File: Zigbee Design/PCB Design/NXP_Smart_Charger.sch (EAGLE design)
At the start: 91 parts, among them IC1 MID400, IC2 MID400, IC3 LMV358, IC4 LMV358, Q1 2222A, Q2 2222A

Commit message: NXP fixes
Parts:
- removed BUTTONS: (no value), SparkFun-Connectors:CONN_04
- removed LEDS: (no value), SparkFun-Connectors:CONN_10"
- removed R32: 2.0k, SparkFun-Resistors:2.0KOHM-0603-1/10W-5%
- removed R37, R38, R39, R40: 10, SparkFun-Resistors:10OHM-0603-1/10W-1%
- removed R42, R43: 75, SparkFun-Resistors:75KOHM-0603-1/10W-1%
- added J4: (no value), SparkFun-Connectors:CONN_08"
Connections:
- removed net CLK: JN5168.DIO16
- removed net FORCE_START: BUTTONS.1, JN5168.DIO0, R34.1
- removed net FORCE_STOP: BUTTONS.2, JN5168.DIO1, R32.1
- removed net L7: R39.2
- removed net L8: R40.2
- removed net N$18: LEDS.7, R37.1
- removed net N$46: JN5168.DIO9
- removed net N$47: JN5168.DIO10
- removed net N$50: LEDS.6, R38.1
- removed net N$51: LEDS.5, R42.1
- removed net N$52: LEDS.4, R39.1
- removed net N$54: LEDS.2, R43.1
- removed net N$55: JN5168.RESETN
- removed net N$56: JN5168.DIO13
- removed net N$75: LEDS.3, R40.1
- removed net SDA: JN5168.DIO17
- new net BUTTON1: J4.5, JN5168.DIO0, R31.1
- new net BUTTON2: J4.4, JN5168.DIO1, R34.1
- net BUTTON3: no longer BUTTONS.3, R31.1
- net GND: now also J4.1; no longer LEDS.1, R32.2
- net L1: now also JN5168.DIO17
- net L2: now also JN5168.DIO16
- net L3: now also JN5168.RESETN
- net L4: now also JN5168.DIO13; no longer R37.2
- net L5: now also JN5168.DIO10; no longer R38.2
- net L6: now also JN5168.DIO9; no longer R42.2
- net L9: no longer R43.2
- net N$14: now also J4.8; no longer LEDS.10
- net N$15: now also J4.7; no longer LEDS.9
- net N$16: now also J4.6; no longer LEDS.8
- net N$93: now also J4.2; no longer BUTTONS.4
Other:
- moved on the sheet: R31, R34, R35

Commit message: changes
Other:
- note removed: "Check power lines on board are correct thickness- especially 3v and GND"
- note removed: "DOUBLE CHECK TX/RX WIRING"
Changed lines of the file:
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@@
 <text x="-165.6" y="38.12" size="3.81" layer="94">for NXP JN5169</text>
 <text x="-119.38" y="223.52" size="6.4516" layer="94">NXP JN5168 Module</text>
-<text x="-73.66" y="160.02" size="1.778" layer="91">DOUBLE CHECK TX/RX WIRING</text>
-<text x="-236.22" y="154.94" size="1.778" layer="91">Check power lines on board are correct thickness- especially 3v and GND</text>
 </plain>
 <instances>
@@
 <pinref part="JN5168" gate="G$1" pin="DIO16"/>
 <wire x1="-91.44" y1="205.74" x2="-78.74" y2="205.74" width="0.1524" layer="91"/>
+<label x="-86.36" y="205.74" size="1.778" layer="95"/>
 </segment>
 </net>
@@
 <pinref part="JN5168" gate="G$1" pin="DIO17"/>
 <wire x1="-91.44" y1="208.28" x2="-78.74" y2="208.28" width="0.1524" layer="91"/>
+<label x="-86.36" y="208.28" size="1.778" layer="95"/>
 </segment>
 </net>
@@
 <pinref part="JN5168" gate="G$1" pin="DIO9"/>
 <wire x1="-104.14" y1="177.8" x2="-104.14" y2="170.18" width="0.1524" layer="91"/>
-<label x="-104.14" y="167.64" size="1.778" layer="95" rot="R90"/>
 </segment>
 </net>
@@
 <pinref part="JN5168" gate="G$1" pin="DIO10"/>
 <wire x1="-101.6" y1="177.8" x2="-101.6" y2="170.18" width="0.1524" layer="91"/>
-<label x="-101.6" y="167.64" size="1.778" layer="95" rot="R90"/>
 </segment>
 </net>
@@
 <pinref part="JN5168" gate="G$1" pin="DIO13"/>
 <wire x1="-91.44" y1="195.58" x2="-81.28" y2="195.58" width="0.1524" layer="91"/>
-<label x="-86.36" y="195.58" size="1.778" layer="95"/>
-</segment>
-</net>
+</segment>
+</net>

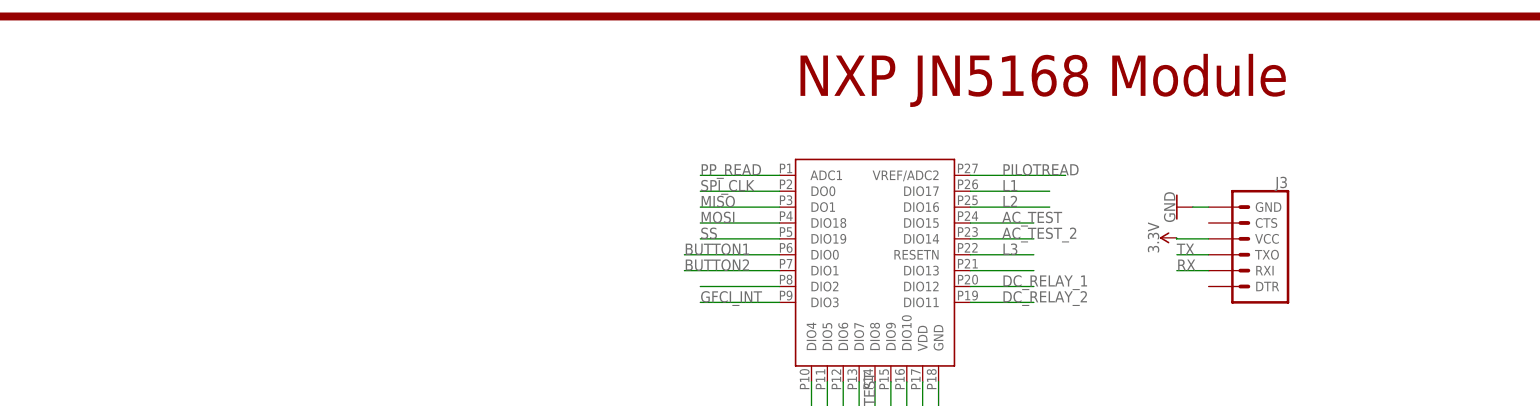
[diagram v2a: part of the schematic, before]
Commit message: added flash memory
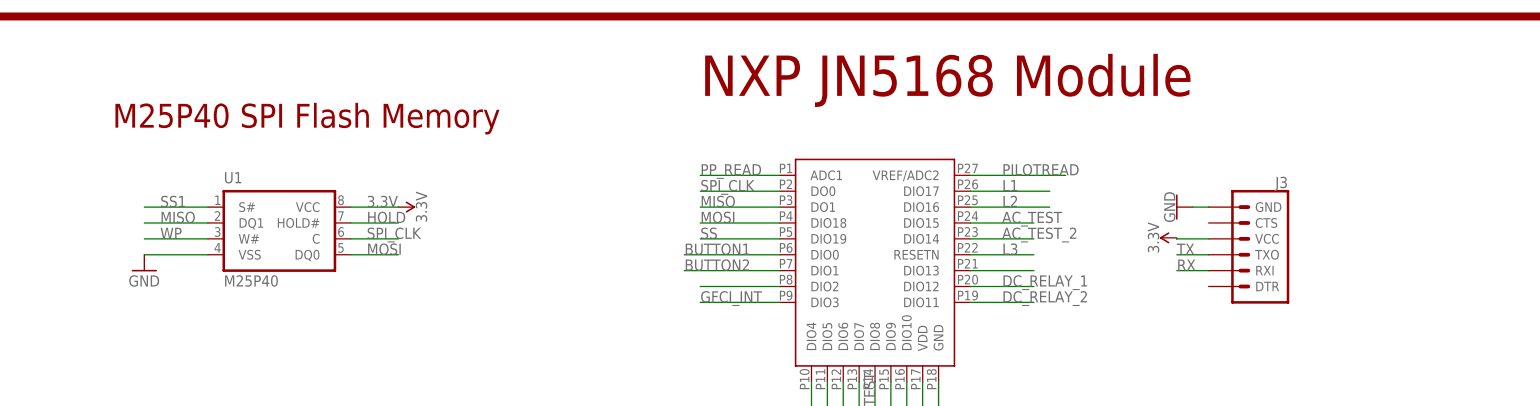
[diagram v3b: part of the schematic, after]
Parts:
- added U1: M25P40, Smart_Charger:M25P40
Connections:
- new net HOLD: U1.HOLD#
- new net SS1: U1.S#
- new net WP: U1.W#
- net 3.3V: now also U1.VCC
- net GND: now also U1.VSS
- net MISO: now also U1.DQ1
- net MOSI: now also U1.DQ0
- net SPI_CLK: now also U1.C
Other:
- note added: "M25P40 SPI Flash Memory"
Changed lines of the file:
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@@
 <part name="SUPPLY4" library="SparkFun-PowerSymbols" deviceset="3.3V" device=""/>
 <part name="J4" library="SparkFun-Connectors" deviceset="CONN_08" device="&quot;"/>
+<part name="U1" library="Smart_Charger" deviceset="M25P40" device=""/>
+<part name="SUPPLY1" library="SparkFun-PowerSymbols" deviceset="3.3V" device=""/>
+<part name="GND7" library="supply1" library_urn="urn:adsk.eagle:library:371" deviceset="GND" device=""/>
 </parts>
 <sheets>
@@
 Extended from Open EVSE project by Chris Howell</text>
 <text x="-165.6" y="38.12" size="3.81" layer="94">for NXP JN5169</text>
-<text x="-119.38" y="223.52" size="6.4516" layer="94">NXP JN5168 Module</text>
+<text x="-134.62" y="223.52" size="6.4516" layer="94">NXP JN5168 Module</text>
+<text x="-228.6" y="218.44" size="3.81" layer="94">M25P40 SPI Flash Memory</text>
 </plain>
 <instances>
@@
 <instance part="SUPPLY4" gate="G$1" x="-99.06" y="170.18" rot="R180"/>
 <instance part="J4" gate="G$1" x="-238.76" y="43.18"/>
+<instance part="U1" gate="G$1" x="-203.2" y="203.2"/>
+<instance part="SUPPLY1" gate="G$1" x="-182.88" y="205.74" rot="R270"/>
+<instance part="GND7" gate="1" x="-223.52" y="195.58"/>
 </instances>
 <busses>
@@
 <label x="-134.62" y="205.74" size="1.778" layer="95"/>
 </segment>
+<segment>
+<pinref part="U1" gate="G$1" pin="DQ1"/>
+<wire x1="-213.36" y1="203.2" x2="-223.52" y2="203.2" width="0.1524" layer="91"/>
+<label x="-220.98" y="203.2" size="1.778" layer="95"/>
+</segment>
 </net>
 <net name="MOSI" class="0">
@@
 <wire x1="-121.92" y1="203.2" x2="-134.62" y2="203.2" width="0.1524" layer="91"/>
 <label x="-134.62" y="203.2" size="1.778" layer="95"/>
+</segment>
+<segment>
+<pinref part="U1" gate="G$1" pin="DQ0"/>
+<wire x1="-190.5" y1="198.12" x2="-182.88" y2="198.12" width="0.1524" layer="91"/>
+<label x="-187.96" y="198.12" size="1.778" layer="95"/>
 </segment>
 </net>
@@
 <wire x1="-231.14" y1="35.56" x2="-231.14" y2="33.02" width="0.1524" layer="91"/>
 </segment>
+<segment>
+<pinref part="U1" gate="G$1" pin="VSS"/>
+<wire x1="-213.36" y1="198.12" x2="-223.52" y2="198.12" width="0.1524" layer="91"/>
+<pinref part="GND7" gate="1" pin="GND"/>
+</segment>
 </net>
 <net name="BUTTON3" class="0">
@@
 <wire x1="-99.06" y1="177.8" x2="-99.06" y2="170.18" width="0.1524" layer="91"/>
 <pinref part="SUPPLY4" gate="G$1" pin="3.3V"/>
+</segment>
+<segment>
+<pinref part="U1" gate="G$1" pin="VCC"/>
+<wire x1="-190.5" y1="205.74" x2="-182.88" y2="205.74" width="0.1524" layer="91"/>
+<label x="-187.96" y="205.74" size="1.778" layer="95"/>
+<pinref part="SUPPLY1" gate="G$1" pin="3.3V"/>
 </segment>
 </net>
@@
 <pinref part="WATTMETER" gate="G$1" pin="3"/>
 </segment>
+<segment>
+<pinref part="U1" gate="G$1" pin="C"/>
+<wire x1="-190.5" y1="200.66" x2="-182.88" y2="200.66" width="0.1524" layer="91"/>
+<label x="-187.96" y="200.66" size="1.778" layer="95"/>
+</segment>
 </net>
 <net name="L6" class="0">
@@
 </segment>
 </net>
+<net name="HOLD" class="0">
+<segment>
+<pinref part="U1" gate="G$1" pin="HOLD#"/>
+<wire x1="-190.5" y1="203.2" x2="-182.88" y2="203.2" width="0.1524" layer="91"/>
+<label x="-187.96" y="203.2" size="1.778" layer="95"/>
+</segment>
+</net>
+<net name="SS1" class="0">
+<segment>
+<pinref part="U1" gate="G$1" pin="S#"/>
+<wire x1="-213.36" y1="205.74" x2="-223.52" y2="205.74" width="0.1524" layer="91"/>
+<label x="-220.98" y="205.74" size="1.778" layer="95"/>
+</segment>
+</net>
+<net name="WP" class="0">
+<segment>
+<pinref part="U1" gate="G$1" pin="W#"/>
+<wire x1="-213.36" y1="200.66" x2="-223.52" y2="200.66" width="0.1524" layer="91"/>
+<label x="-220.98" y="200.66" size="1.778" layer="95"/>
+</segment>
+</net>

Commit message: added smartenit eagle file
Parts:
- removed J3: (no value), SparkFun-Connectors:6_PIN_SERIAL_TARGET
- removed U1: M25P40, Smart_Charger:M25P40
- added U$1: SPI_FLASH-X25XXSMD, SparkFun:SPI_FLASH-X25XXSMD
- added U$2: AVR_SPI_PROG2LOCK, SparkFun:AVR_SPI_PROG2LOCK
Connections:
- removed net BUTTON3: JN5168.DIO2
- removed net HOLD: U1.HOLD#
- removed net L4: JN5168.DIO13
- removed net L5: JN5168.DIO10
- removed net L6: JN5168.DIO9
- removed net L9: JN5168.DIO4
- removed net WP: U1.W#
- new net RESET: JN5168.RESETN
- net 3.3V: now also JN5168.VREF/ADC2, U$1.WP; no longer J3.VCC, U1.VCC
- net GND: now also U$1.GND; no longer J3.GND, U1.VSS
- net L3: now also JN5168.DIO13; no longer JN5168.RESETN
- net MISO: now also U$1.MISO; no longer U1.DQ1
- net MOSI: no longer U1.DQ0
- net PILOTREAD: now also JN5168.DIO2; no longer JN5168.VREF/ADC2
- net RX: no longer J3.RXI
- net SPI_CLK: no longer U1.C
- net SS1: now also JN5168.DIO4, U$1.CS; no longer U1.S#
- net TX: no longer J3.TXO
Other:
- note added: "W25X40CLSNIG-ND SPI Flash Memory"
- note removed: "M25P40 SPI Flash Memory"
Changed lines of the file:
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@@
 <part name="J2" library="SparkFun-Connectors" deviceset="CONN_02" device=""/>
 <part name="DC2" library="DCDCconverters" deviceset="NNM+-12V" device=""/>
-<part name="J3" library="SparkFun-Connectors" deviceset="6_PIN_SERIAL_TARGET" device=""/>
-<part name="SUPPLY3" library="SparkFun-PowerSymbols" deviceset="3.3V" device=""/>
-<part name="GND37" library="SparkFun-PowerSymbols" deviceset="GND" device=""/>
 <part name="JN5168" library="Smart_Charger" deviceset="NXP_JN5168-001-MO3" device=""/>
 <part name="GND6" library="supply1" library_urn="urn:adsk.eagle:library:371" deviceset="GND" device=""/>
 <part name="SUPPLY4" library="SparkFun-PowerSymbols" deviceset="3.3V" device=""/>
 <part name="J4" library="SparkFun-Connectors" deviceset="CONN_08" device="&quot;"/>
-<part name="U1" library="Smart_Charger" deviceset="M25P40" device=""/>
 <part name="SUPPLY1" library="SparkFun-PowerSymbols" deviceset="3.3V" device=""/>
 <part name="GND7" library="supply1" library_urn="urn:adsk.eagle:library:371" deviceset="GND" device=""/>
+<part name="SUPPLY6" library="SparkFun-PowerSymbols" deviceset="3.3V" device=""/>
+<part name="U$1" library="SparkFun" deviceset="SPI_FLASH-X25XX" device="SMD"/>
+<part name="SUPPLY9" library="SparkFun-PowerSymbols" deviceset="3.3V" device=""/>
+<part name="SUPPLY10" library="SparkFun-PowerSymbols" deviceset="3.3V" device=""/>
+<part name="U$2" library="SparkFun" deviceset="AVR_SPI_PROG2" device="LOCK"/>
 </parts>
 <sheets>
@@
 <text x="-165.6" y="38.12" size="3.81" layer="94">for NXP JN5169</text>
 <text x="-134.62" y="223.52" size="6.4516" layer="94">NXP JN5168 Module</text>
-<text x="-228.6" y="218.44" size="3.81" layer="94">M25P40 SPI Flash Memory</text>
+<text x="-228.6" y="218.44" size="3.81" layer="94">W25X40CLSNIG-ND SPI Flash Memory</text>
 </plain>
 <instances>
@@
 <instance part="J2" gate="G$1" x="36.5" y="-0.3"/>
 <instance part="DC2" gate="&gt;NAME" x="87.7" y="217.1"/>
-<instance part="J3" gate="G$1" x="-48.26" y="198.12" rot="MR0"/>
-<instance part="SUPPLY3" gate="G$1" x="-58.46" y="200.82" rot="R90"/>
-<instance part="GND37" gate="1" x="-58.42" y="205.74" rot="R270"/>
 <instance part="JN5168" gate="G$1" x="-78.74" y="190.5"/>
 <instance part="GND6" gate="1" x="-96.52" y="157.48"/>
 <instance part="SUPPLY4" gate="G$1" x="-99.06" y="170.18" rot="R180"/>
 <instance part="J4" gate="G$1" x="-238.76" y="43.18"/>
-<instance part="U1" gate="G$1" x="-203.2" y="203.2"/>
-<instance part="SUPPLY1" gate="G$1" x="-182.88" y="205.74" rot="R270"/>
+<instance part="SUPPLY1" gate="G$1" x="-175.26" y="205.74" rot="R270"/>
 <instance part="GND7" gate="1" x="-223.52" y="195.58"/>
+<instance part="SUPPLY6" gate="G$1" x="-76.2" y="210.82" rot="R270"/>
+<instance part="U$1" gate="G$1" x="-198.12" y="203.2"/>
+<instance part="SUPPLY9" gate="G$1" x="-223.52" y="200.66" rot="R90"/>
+<instance part="SUPPLY10" gate="G$1" x="-175.26" y="203.2" rot="R270"/>
+<instance part="U$2" gate="A" x="-45.72" y="175.26"/>
 </instances>
 <busses>
@@
 </segment>
 <segment>
-<pinref part="JN5168" gate="G$1" pin="VREF/ADC2"/>
-<wire x1="-91.44" y1="210.82" x2="-76.2" y2="210.82" width="0.1524" layer="91"/>
-<label x="-86.36" y="210.82" size="1.778" layer="95"/>
+<pinref part="JN5168" gate="G$1" pin="DIO2"/>
+<wire x1="-121.92" y1="193.04" x2="-134.62" y2="193.04" width="0.1524" layer="91"/>
+<label x="-137.16" y="193.04" size="1.778" layer="95"/>
 </segment>
 </net>
@@
 </segment>
 <segment>
-<pinref part="U1" gate="G$1" pin="DQ1"/>
 <wire x1="-213.36" y1="203.2" x2="-223.52" y2="203.2" width="0.1524" layer="91"/>
 <label x="-220.98" y="203.2" size="1.778" layer="95"/>
+<pinref part="U$1" gate="G$1" pin="MISO"/>
 </segment>
 </net>
@@
 </segment>
 <segment>
-<pinref part="U1" gate="G$1" pin="DQ0"/>
-<wire x1="-190.5" y1="198.12" x2="-182.88" y2="198.12" width="0.1524" layer="91"/>
-<label x="-187.96" y="198.12" size="1.778" layer="95"/>
+<wire x1="-182.88" y1="198.12" x2="-175.26" y2="198.12" width="0.1524" layer="91"/>
+<label x="-180.34" y="198.12" size="1.778" layer="95"/>
 </segment>
 </net>
@@
 </segment>
 <segment>
-<pinref part="GND37" gate="1" pin="GND"/>
-<pinref part="J3" gate="G$1" pin="GND"/>
-<wire x1="-55.88" y1="205.74" x2="-53.34" y2="205.74" width="0.1524" layer="91"/>
-</segment>
-<segment>
 <pinref part="JN5168" gate="G$1" pin="GND"/>
 <wire x1="-96.52" y1="177.8" x2="-96.52" y2="160.02" width="0.1524" layer="91"/>
@@
 </segment>
 <segment>
-<pinref part="U1" gate="G$1" pin="VSS"/>
 <wire x1="-213.36" y1="198.12" x2="-223.52" y2="198.12" width="0.1524" layer="91"/>
 <pinref part="GND7" gate="1" pin="GND"/>
-</segment>
-</net>
-<net name="BUTTON3" class="0">
-<segment>
-<pinref part="JN5168" gate="G$1" pin="DIO2"/>
-<wire x1="-121.92" y1="193.04" x2="-134.62" y2="193.04" width="0.1524" layer="91"/>
+<pinref part="U$1" gate="G$1" pin="GND"/>
 </segment>
 </net>
@@
 </segment>
 </net>
-<net name="L9" class="0">
-<segment>
-<pinref part="JN5168" gate="G$1" pin="DIO4"/>
-<wire x1="-116.84" y1="177.8" x2="-116.84" y2="170.18" width="0.1524" layer="91"/>
-</segment>
-</net>
 <net name="L3" class="0">
 <segment>
@@
 </segment>
 <segment>
-<pinref part="JN5168" gate="G$1" pin="RESETN"/>
-<wire x1="-91.44" y1="198.12" x2="-81.28" y2="198.12" width="0.1524" layer="91"/>
-<label x="-86.36" y="198.12" size="1.778" layer="95"/>
+<pinref part="JN5168" gate="G$1" pin="DIO13"/>
+<wire x1="-91.44" y1="195.58" x2="-81.28" y2="195.58" width="0.1524" layer="91"/>
+<label x="-86.36" y="195.58" size="1.778" layer="95"/>
 </segment>
 </net>
@@
 </segment>
 <segment>
-<pinref part="SUPPLY3" gate="G$1" pin="3.3V"/>
-<pinref part="J3" gate="G$1" pin="VCC"/>
-<wire x1="-58.46" y1="200.82" x2="-58.46" y2="200.66" width="0.1524" layer="91"/>
-<wire x1="-58.46" y1="200.66" x2="-53.34" y2="200.66" width="0.1524" layer="91"/>
-</segment>
-<segment>
 <pinref part="JN5168" gate="G$1" pin="VDD"/>
 <wire x1="-99.06" y1="177.8" x2="-99.06" y2="170.18" width="0.1524" layer="91"/>
@@
 </segment>
 <segment>
-<pinref part="U1" gate="G$1" pin="VCC"/>
-<wire x1="-190.5" y1="205.74" x2="-182.88" y2="205.74" width="0.1524" layer="91"/>
-<label x="-187.96" y="205.74" size="1.778" layer="95"/>
+<wire x1="-182.88" y1="205.74" x2="-175.26" y2="205.74" width="0.1524" layer="91"/>
+<label x="-180.34" y="205.74" size="1.778" layer="95"/>
 <pinref part="SUPPLY1" gate="G$1" pin="3.3V"/>
+</segment>
+<segment>
+<pinref part="JN5168" gate="G$1" pin="VREF/ADC2"/>
+<wire x1="-91.44" y1="210.82" x2="-76.2" y2="210.82" width="0.1524" layer="91"/>
+<label x="-86.36" y="210.82" size="1.778" layer="95"/>
+<pinref part="SUPPLY6" gate="G$1" pin="3.3V"/>
+</segment>
+<segment>
+<wire x1="-213.36" y1="200.66" x2="-223.52" y2="200.66" width="0.1524" layer="91"/>
+<label x="-220.98" y="200.66" size="1.778" layer="95"/>
+<pinref part="U$1" gate="G$1" pin="WP"/>
+<pinref part="SUPPLY9" gate="G$1" pin="3.3V"/>
+</segment>
+<segment>
+<wire x1="-182.88" y1="203.2" x2="-175.26" y2="203.2" width="0.1524" layer="91"/>
+<label x="-180.34" y="203.2" size="1.778" layer="95"/>
+<pinref part="SUPPLY10" gate="G$1" pin="3.3V"/>
 </segment>
 </net>
@@
 <label x="-111.76" y="167.64" size="1.778" layer="95" rot="R90"/>
 </segment>
-<segment>
-<pinref part="J3" gate="G$1" pin="TXO"/>
-<wire x1="-53.34" y1="198.12" x2="-58.42" y2="198.12" width="0.1524" layer="91"/>
-<label x="-58.42" y="198.12" size="1.778" layer="95"/>
-</segment>
 </net>
 <net name="RX" class="0">
@@
 <label x="-109.22" y="167.64" size="1.778" layer="95" rot="R90"/>
 </segment>
-<segment>
-<pinref part="J3" gate="G$1" pin="RXI"/>
-<wire x1="-53.34" y1="195.58" x2="-58.42" y2="195.58" width="0.1524" layer="91"/>
-<label x="-58.42" y="195.58" size="1.778" layer="95"/>
-</segment>
 </net>
 <net name="SPI_CLK" class="0">
@@
 </segment>
 <segment>
-<pinref part="U1" gate="G$1" pin="C"/>
-<wire x1="-190.5" y1="200.66" x2="-182.88" y2="200.66" width="0.1524" layer="91"/>
-<label x="-187.96" y="200.66" size="1.778" layer="95"/>
-</segment>
-</net>
-<net name="L6" class="0">
-<segment>
-<pinref part="JN5168" gate="G$1" pin="DIO9"/>
-<wire x1="-104.14" y1="177.8" x2="-104.14" y2="170.18" width="0.1524" layer="91"/>
-</segment>
-</net>
-<net name="L5" class="0">
-<segment>
-<pinref part="JN5168" gate="G$1" pin="DIO10"/>
-<wire x1="-101.6" y1="177.8" x2="-101.6" y2="170.18" width="0.1524" layer="91"/>
-</segment>
-</net>
-<net name="L4" class="0">
-<segment>
-<pinref part="JN5168" gate="G$1" pin="DIO13"/>
-<wire x1="-91.44" y1="195.58" x2="-81.28" y2="195.58" width="0.1524" layer="91"/>
+<wire x1="-182.88" y1="200.66" x2="-175.26" y2="200.66" width="0.1524" layer="91"/>
+<label x="-180.34" y="200.66" size="1.778" layer="95"/>
 </segment>
 </net>
@@
 </segment>
 </net>
-<net name="HOLD" class="0">
-<segment>
-<pinref part="U1" gate="G$1" pin="HOLD#"/>
-<wire x1="-190.5" y1="203.2" x2="-182.88" y2="203.2" width="0.1524" layer="91"/>
-<label x="-187.96" y="203.2" size="1.778" layer="95"/>
-</segment>
-</net>
 <net name="SS1" class="0">
 <segment>
-<pinref part="U1" gate="G$1" pin="S#"/>
 <wire x1="-213.36" y1="205.74" x2="-223.52" y2="205.74" width="0.1524" layer="91"/>
 <label x="-220.98" y="205.74" size="1.778" layer="95"/>
-</segment>
-</net>
-<net name="WP" class="0">
-<segment>
-<pinref part="U1" gate="G$1" pin="W#"/>
-<wire x1="-213.36" y1="200.66" x2="-223.52" y2="200.66" width="0.1524" layer="91"/>
-<label x="-220.98" y="200.66" size="1.778" layer="95"/>
-</segment>
-</net>
+<pinref part="U$1" gate="G$1" pin="CS"/>
+</segment>
+<segment>
+<pinref part="JN5168" gate="G$1" pin="DIO4"/>
+<wire x1="-116.84" y1="177.8" x2="-116.84" y2="170.18" width="0.1524" layer="91"/>
+<label x="-116.84" y="170.18" size="1.778" layer="95" rot="R90"/>
+</segment>
+</net>
+<net name="RESET" class="0">
+<segment>
+<pinref part="JN5168" gate="G$1" pin="RESETN"/>
+<wire x1="-91.44" y1="198.12" x2="-81.28" y2="198.12" width="0.1524" layer="91"/>
+<label x="-86.36" y="198.12" size="1.778" layer="95"/>
+</segment>
+</net>
